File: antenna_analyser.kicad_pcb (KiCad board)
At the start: 2 copper layers, 100 x 50 mm, 32 parts, among them IC1 MCP6002, IC2 ARDUINO_PRO_MINI_3.3V, P1 AD9850_CONN, P2 BNC, P3 CONN_LCD, P4 USB_OTG, P5 CONN_PROG, U1 AMS1117

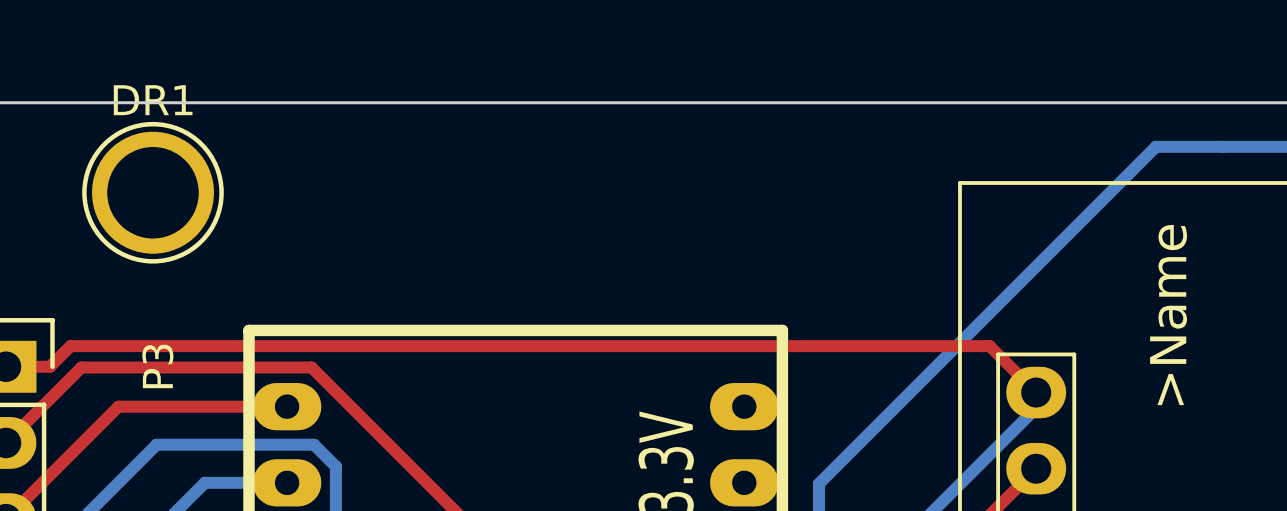
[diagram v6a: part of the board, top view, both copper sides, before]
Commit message: Added a shortlink to the github site:
http://j.mp/HFAA9850
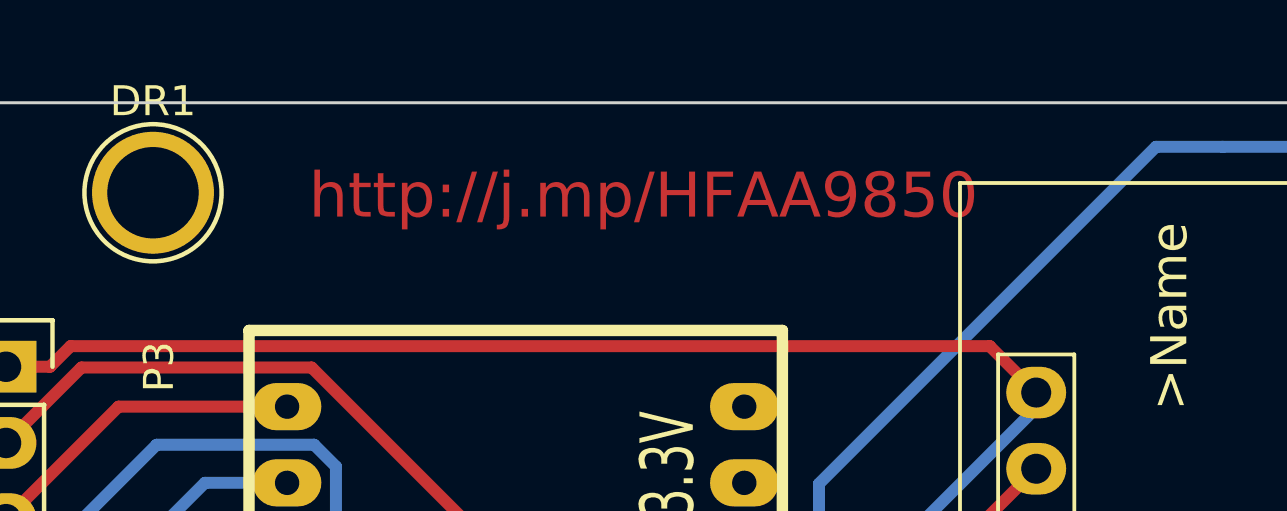
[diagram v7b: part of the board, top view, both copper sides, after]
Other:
- board text added: "http://j.mp/HFAA9850"
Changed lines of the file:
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@@
     (area 89.949999 83.949999 190.050001 134.050001)
     (thickness 1.6)
-    (drawings 8)
+    (drawings 9)
     (tracks 291)
     (zones 0)
@@
     )
   )
+  (gr_text http://j.mp/HFAA9850 (at 113.35 87.1) (layer F.Cu)
+    (effects (font (size 1.5 1.5) (thickness 0.3)))
+  )
   (dimension 7 (width 0.3) (layer Dwgs.User)

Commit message: A few mods more.
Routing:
- net Net-(IC1-Pad7): track 93.9 -> 137.3 mm
- net GND: track 246.9 -> 248.8 mm
- net Net-(IC1-Pad1): track 70.1 -> 71.6 mm
- net +5V: track 147.2 -> 147.8 mm
